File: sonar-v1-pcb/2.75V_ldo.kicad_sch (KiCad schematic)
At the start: 5 parts, among them U4 AP2127K-ADJTRG1

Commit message: Make some small visual edits
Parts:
- renumbered C2 to C1, C5 to C2, R8 to R1, R7 to R2, U4 to U1
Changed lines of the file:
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@@
 		)
 		(instances
+			(project "tx-rx-dev-board"
+				(path "/ef969c50-8ad8-46a7-babe-de0c0ef3b48a/a1ce93bf-af3c-4f98-981d-799fe49a13ba"
+					(reference "#PWR019")
+					(unit 1)
+				)
+			)
 			(project "sonar"
 				(path "/f72ceae0-eee4-4385-b0e8-639846bcb5f2/0971c334-b681-41ae-ad35-a89520df0687/ee73137f-d5eb-4789-88c4-4482e951aa01"
@@
 		)
 		(instances
+			(project "tx-rx-dev-board"
+				(path "/ef969c50-8ad8-46a7-babe-de0c0ef3b48a/a1ce93bf-af3c-4f98-981d-799fe49a13ba"
+					(reference "#PWR017")
+					(unit 1)
+				)
+			)
 			(project "sonar"
 				(path "/f72ceae0-eee4-4385-b0e8-639846bcb5f2/0971c334-b681-41ae-ad35-a89520df0687/ee73137f-d5eb-4789-88c4-4482e951aa01"
@@
 		)
 		(instances
+			(project "tx-rx-dev-board"
+				(path "/ef969c50-8ad8-46a7-babe-de0c0ef3b48a/a1ce93bf-af3c-4f98-981d-799fe49a13ba"
+					(reference "#PWR014")
+					(unit 1)
+				)
+			)
 			(project "sonar"
 				(path "/f72ceae0-eee4-4385-b0e8-639846bcb5f2/0971c334-b681-41ae-ad35-a89520df0687/ee73137f-d5eb-4789-88c4-4482e951aa01"
@@
 		(in_pos_files yes)
 		(dnp no)
-		(property "Reference" "C2"
+		(property "Reference" "C1"
 			(at 71.12 74.9299 0)
 			(show_name no)
@@
 		)
 		(instances
+			(project "tx-rx-dev-board"
+				(path "/ef969c50-8ad8-46a7-babe-de0c0ef3b48a/a1ce93bf-af3c-4f98-981d-799fe49a13ba"
+					(reference "C1")
+					(unit 1)
+				)
+			)
 			(project "sonar"
 				(path "/f72ceae0-eee4-4385-b0e8-639846bcb5f2/0971c334-b681-41ae-ad35-a89520df0687/ee73137f-d5eb-4789-88c4-4482e951aa01"
@@
 		)
 		(instances
+			(project "tx-rx-dev-board"
+				(path "/ef969c50-8ad8-46a7-babe-de0c0ef3b48a/a1ce93bf-af3c-4f98-981d-799fe49a13ba"
+					(reference "#PWR012")
+					(unit 1)
+				)
+			)
 			(project "sonar"
 				(path "/f72ceae0-eee4-4385-b0e8-639846bcb5f2/0971c334-b681-41ae-ad35-a89520df0687/ee73137f-d5eb-4789-88c4-4482e951aa01"
@@
 		)
 		(instances
+			(project "tx-rx-dev-board"
+				(path "/ef969c50-8ad8-46a7-babe-de0c0ef3b48a/a1ce93bf-af3c-4f98-981d-799fe49a13ba"
+					(reference "#PWR015")
+					(unit 1)
+				)
+			)
 			(project "sonar"
 				(path "/f72ceae0-eee4-4385-b0e8-639846bcb5f2/0971c334-b681-41ae-ad35-a89520df0687/ee73137f-d5eb-4789-88c4-4482e951aa01"
@@
 		(in_pos_files yes)
 		(dnp no)
-		(property "Reference" "U4"
+		(property "Reference" "U1"
 			(at 102.87 60.96 0)
 			(show_name no)
@@
 		)
 		(instances
+			(project "tx-rx-dev-board"
+				(path "/ef969c50-8ad8-46a7-babe-de0c0ef3b48a/a1ce93bf-af3c-4f98-981d-799fe49a13ba"
+					(reference "U1")
+					(unit 1)
+				)
+			)
 			(project "sonar"
 				(path "/f72ceae0-eee4-4385-b0e8-639846bcb5f2/0971c334-b681-41ae-ad35-a89520df0687/ee73137f-d5eb-4789-88c4-4482e951aa01"
@@
 		)
 		(instances
+			(project "tx-rx-dev-board"
+				(path "/ef969c50-8ad8-46a7-babe-de0c0ef3b48a/a1ce93bf-af3c-4f98-981d-799fe49a13ba"
+					(reference "#PWR09")
+					(unit 1)
+				)
+			)
 			(project "sonar"
 				(path "/f72ceae0-eee4-4385-b0e8-639846bcb5f2/0971c334-b681-41ae-ad35-a89520df0687/ee73137f-d5eb-4789-88c4-4482e951aa01"
@@
 		(in_pos_files yes)
 		(dnp no)
-		(property "Reference" "C5"
+		(property "Reference" "C2"
 			(at 139.7 74.9299 0)
 			(show_name no)
@@
 		)
 		(instances
+			(project "tx-rx-dev-board"
+				(path "/ef969c50-8ad8-46a7-babe-de0c0ef3b48a/a1ce93bf-af3c-4f98-981d-799fe49a13ba"
+					(reference "C2")
+					(unit 1)
+				)
+			)
 			(project "sonar"
 				(path "/f72ceae0-eee4-4385-b0e8-639846bcb5f2/0971c334-b681-41ae-ad35-a89520df0687/ee73137f-d5eb-4789-88c4-4482e951aa01"
@@
 		(dnp no)
 		(fields_autoplaced yes)
-		(property "Reference" "R8"
+		(property "Reference" "R1"
 			(at 128.27 69.8499 0)
 			(show_name no)
@@
 		)
 		(instances
+			(project "tx-rx-dev-board"
+				(path "/ef969c50-8ad8-46a7-babe-de0c0ef3b48a/a1ce93bf-af3c-4f98-981d-799fe49a13ba"
+					(reference "R1")
+					(unit 1)
+				)
+			)
 			(project "sonar"
 				(path "/f72ceae0-eee4-4385-b0e8-639846bcb5f2/0971c334-b681-41ae-ad35-a89520df0687/ee73137f-d5eb-4789-88c4-4482e951aa01"
@@
 		(dnp no)
 		(fields_autoplaced yes)
-		(property "Reference" "R7"
+		(property "Reference" "R2"
 			(at 128.27 77.4699 0)
 			(show_name no)
@@
 		)
 		(instances
+			(project "tx-rx-dev-board"
+				(path "/ef969c50-8ad8-46a7-babe-de0c0ef3b48a/a1ce93bf-af3c-4f98-981d-799fe49a13ba"
+					(reference "R2")
+					(unit 1)
+				)
+			)
 			(project "sonar"
 				(path "/f72ceae0-eee4-4385-b0e8-639846bcb5f2/0971c334-b681-41ae-ad35-a89520df0687/ee73137f-d5eb-4789-88c4-4482e951aa01"
@@
 		)
 		(instances
+			(project "tx-rx-dev-board"
+				(path "/ef969c50-8ad8-46a7-babe-de0c0ef3b48a/a1ce93bf-af3c-4f98-981d-799fe49a13ba"
+					(reference "#PWR018")
+					(unit 1)
+				)
+			)
 			(project "sonar"
 				(path "/f72ceae0-eee4-4385-b0e8-639846bcb5f2/0971c334-b681-41ae-ad35-a89520df0687/ee73137f-d5eb-4789-88c4-4482e951aa01"

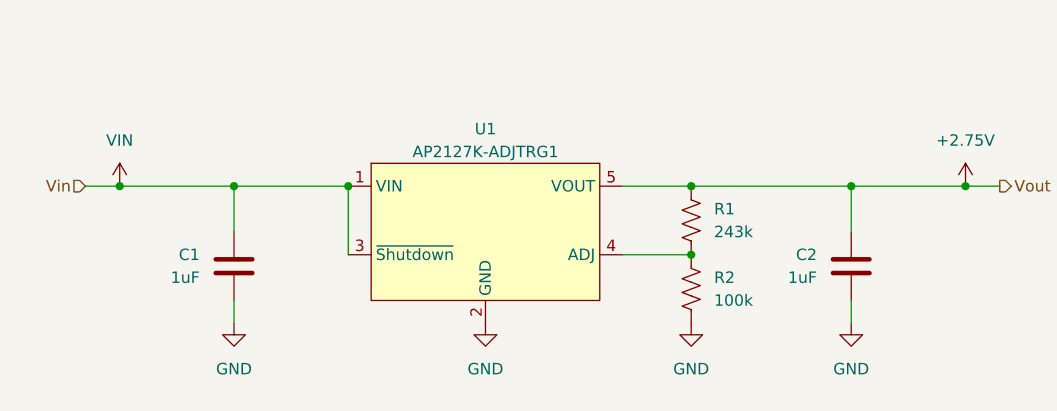
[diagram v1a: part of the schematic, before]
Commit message: Fix some stuff kinda in the short term but this should be fixed long term
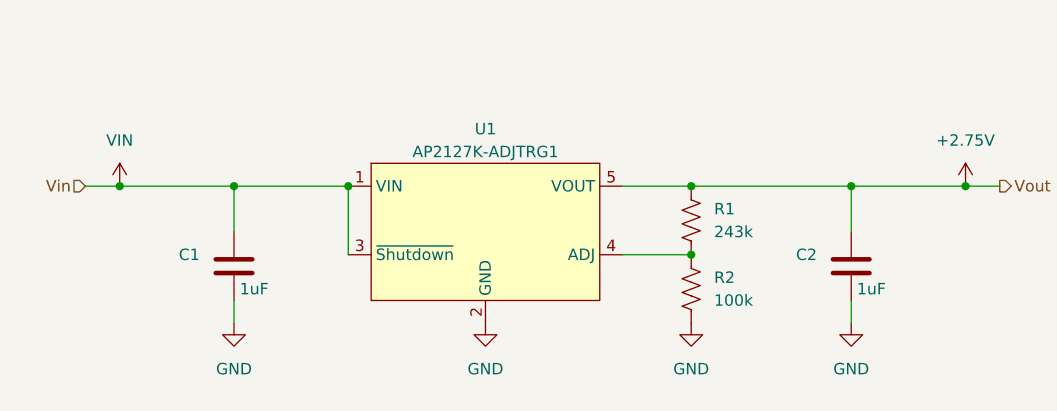
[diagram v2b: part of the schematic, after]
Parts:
- C1, C2: footprint Sonar:C_0603_1608Metric -> GS_Capacitors:C_0603_1608Metric; symbol sonar_lib:C_0603_1uF -> GS_Capacitor_0603:C_0603_1uF
- R2: footprint Sonar:R_0603_1608Metric -> GS_Resistors:R_0603_1608Metric; symbol sonar_lib:R_0603_100k -> GS_Resistor_0603:R_0603_100k; MPN (none) -> RC0603FR-07100KL
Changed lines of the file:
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@@
 	)
 	(symbol
-		(lib_id "sonar_lib:C_0603_1uF")
+		(lib_id "GS_Capacitor_0603:C_0603_1uF")
 		(at 74.93 76.2 0)
 		(unit 1)
@@
 		)
 		(property "Value" "1uF"
-			(at 71.12 77.4699 0)
-			(show_name no)
-			(do_not_autoplace no)
-			(effects
-				(font
-					(size 1.27 1.27)
-				)
-				(justify right)
-			)
-		)
-		(property "Footprint" "Sonar:C_0603_1608Metric"
+			(at 75.565 78.74 0)
+			(show_name no)
+			(do_not_autoplace no)
+			(effects
+				(font
+					(size 1.27 1.27)
+				)
+				(justify left)
+			)
+		)
+		(property "Footprint" "GS_Capacitors:C_0603_1608Metric"
 			(at 74.93 53.848 0)
 			(hide yes)
@@
 	)
 	(symbol
-		(lib_id "sonar_lib:C_0603_1uF")
+		(lib_id "GS_Capacitor_0603:C_0603_1uF")
 		(at 143.51 76.2 0)
 		(unit 1)
@@
 		)
 		(property "Value" "1uF"
-			(at 139.7 77.4699 0)
-			(show_name no)
-			(do_not_autoplace no)
-			(effects
-				(font
-					(size 1.27 1.27)
-				)
-				(justify right)
-			)
-		)
-		(property "Footprint" "Sonar:C_0603_1608Metric"
+			(at 144.145 78.74 0)
+			(show_name no)
+			(do_not_autoplace no)
+			(effects
+				(font
+					(size 1.27 1.27)
+				)
+				(justify left)
+			)
+		)
+		(property "Footprint" "GS_Capacitors:C_0603_1608Metric"
 			(at 143.51 53.848 0)
 			(hide yes)
@@
 	)
 	(symbol
-		(lib_id "sonar_lib:R_0603_100k")
+		(lib_id "GS_Resistor_0603:R_0603_100k")
 		(at 125.73 78.74 0)
 		(unit 1)
@@
 			)
 		)
-		(property "Footprint" "Sonar:R_0603_1608Metric"
+		(property "Footprint" "GS_Resistors:R_0603_1608Metric"
 			(at 125.73 56.642 0)
 			(hide yes)
@@
 			(hide yes)
 			(show_name no)
+			(do_not_autoplace no)
+			(effects
+				(font
+					(size 1.27 1.27)
+				)
+			)
+		)
+		(property "MPN" "RC0603FR-07100KL"
+			(at 125.73 54.102 0)
+			(hide yes)
+			(show_name no)

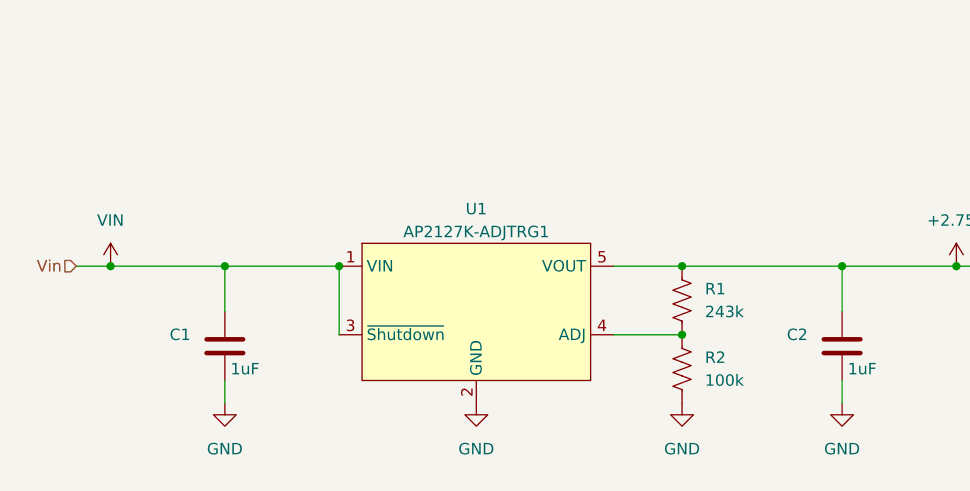
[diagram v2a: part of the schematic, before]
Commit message: Add an h-bridge
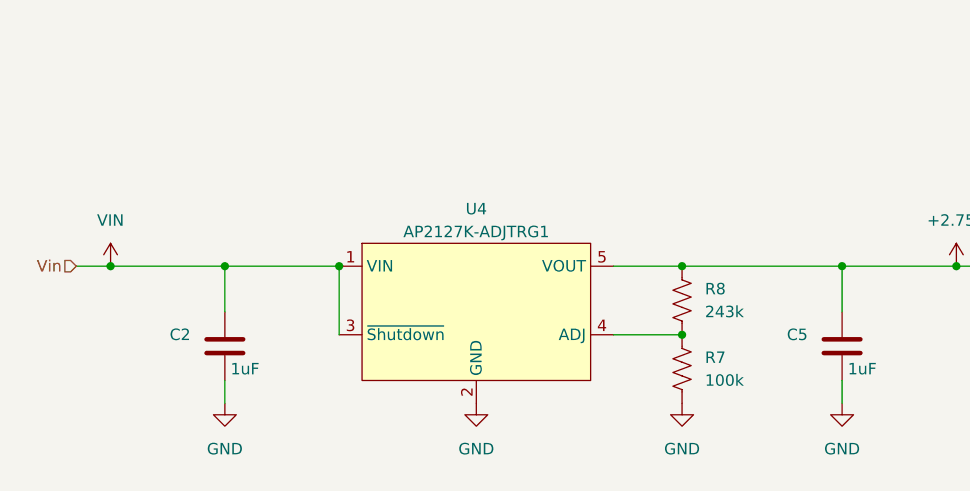
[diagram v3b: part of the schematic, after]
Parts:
- renumbered C1 to C2, C2 to C5, R2 to R7, R1 to R8, U1 to U4
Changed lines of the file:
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@@
 		(in_pos_files yes)
 		(dnp no)
-		(property "Reference" "C1"
+		(property "Reference" "C2"
 			(at 71.12 74.9299 0)
 			(show_name no)
@@
 		(in_pos_files yes)
 		(dnp no)
-		(property "Reference" "U1"
+		(property "Reference" "U4"
 			(at 102.87 60.96 0)
 			(show_name no)
@@
 		(in_pos_files yes)
 		(dnp no)
-		(property "Reference" "C2"
+		(property "Reference" "C5"
 			(at 139.7 74.9299 0)
 			(show_name no)
@@
 		(dnp no)
 		(fields_autoplaced yes)
-		(property "Reference" "R1"
+		(property "Reference" "R8"
 			(at 128.27 69.8499 0)
 			(show_name no)
@@
 		(dnp no)
 		(fields_autoplaced yes)
-		(property "Reference" "R2"
+		(property "Reference" "R7"
 			(at 128.27 77.4699 0)
 			(show_name no)
